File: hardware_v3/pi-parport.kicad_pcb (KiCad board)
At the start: 2 copper layers, 65 x 56 mm, 17 parts, among them J1 CONN_01X02, J2 40HAT, J3 Conn_02x13_Odd_Even, U1 CAT24C32, U2 SN74LVC161284DLR

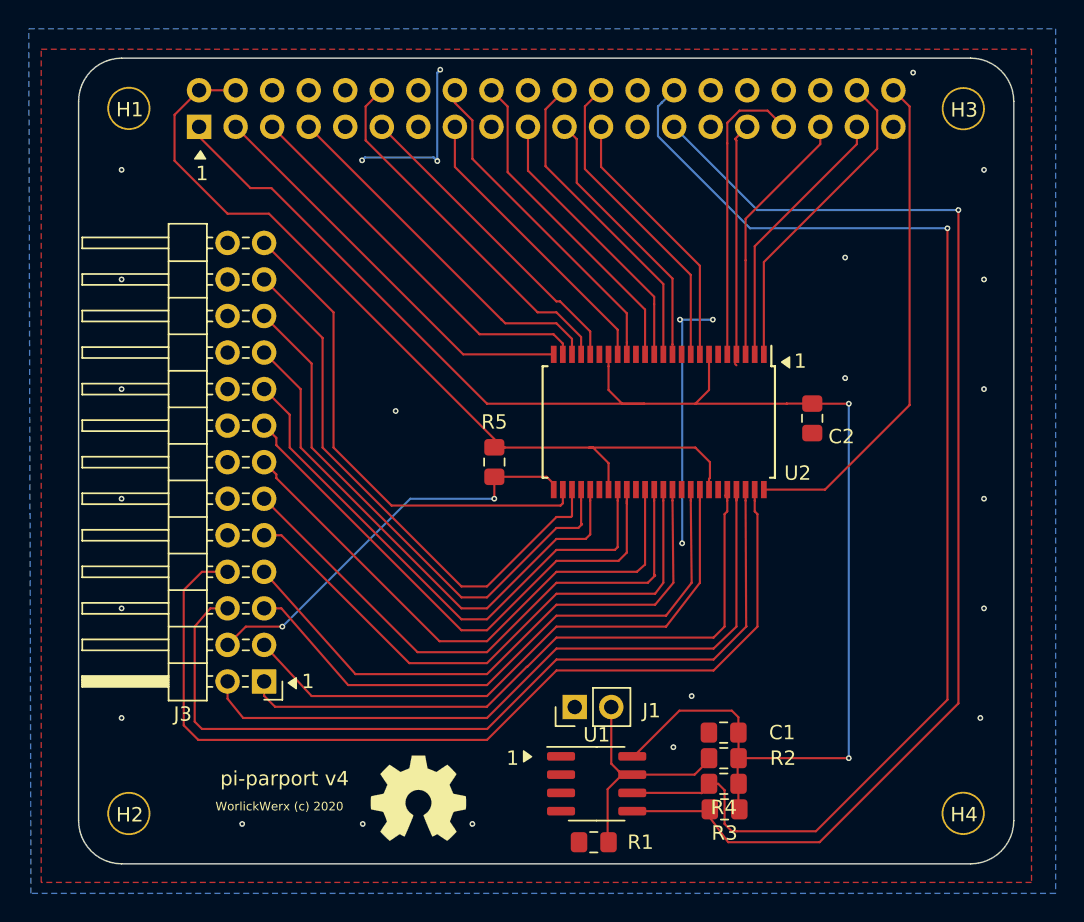
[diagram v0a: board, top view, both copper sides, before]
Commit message: hardware: reroute another under-resistor trace, other cleanup
Fix board edge outline that was just barely not closed.

Fix overlapping courtyards in resistors next to U1.

Move obscured silkscreen reference R4.

Cleanup one tiny trace left over from rerouting.

Change version to v4 in BOM.md.
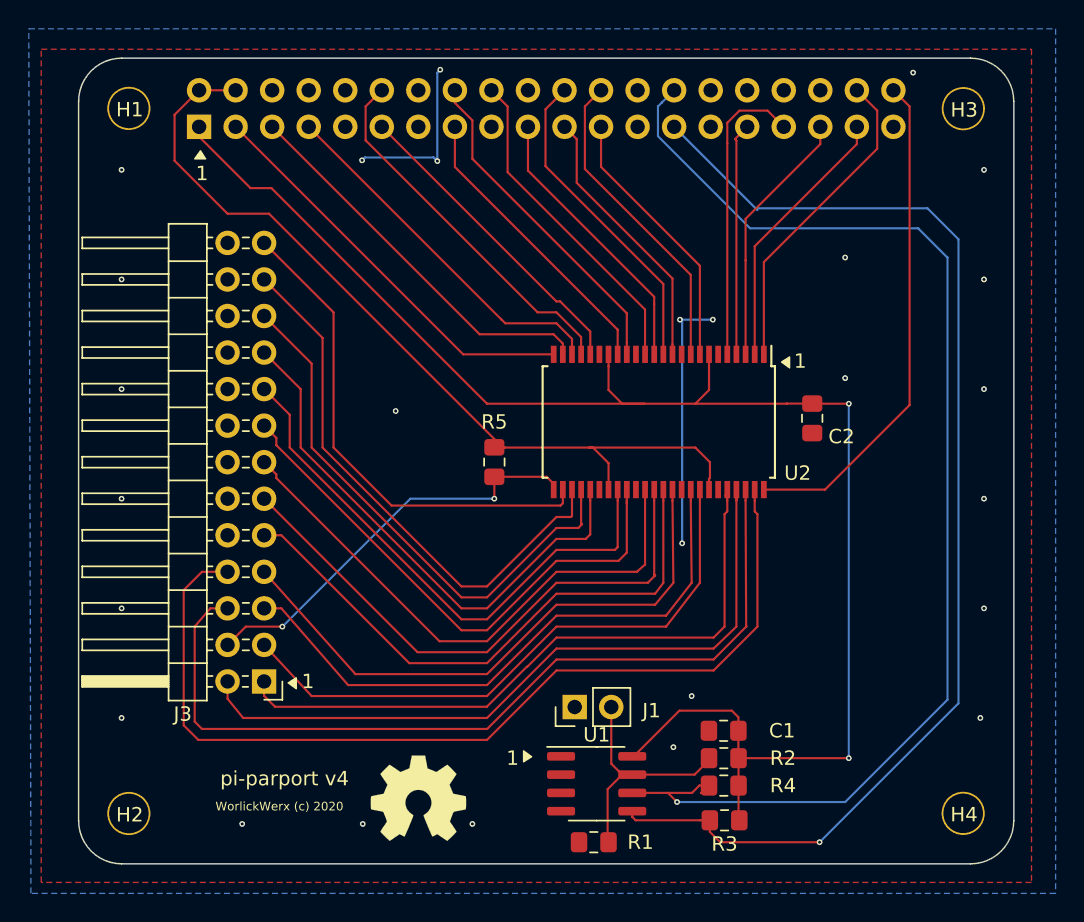
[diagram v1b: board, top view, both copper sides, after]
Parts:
- moved R3 0.76 mm to (123.4, 113.8)
- moved R4 0.13 mm to (123.4, 111.4)
- moved C1 0.13 mm to (123.4, 107.6)
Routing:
- net /ID_SC_EEPROM: track 87.8 -> 86.2 mm
- net +3V3: track 110.2 -> 111.1 mm
- net /ID_SD_EEPROM: track 85.7 -> 84.9 mm
